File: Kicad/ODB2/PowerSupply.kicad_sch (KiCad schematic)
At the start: 54 parts, among them J2 Batt4v2, J3 Batt7V4, Q3 PJA3411_R1_00001, U2 TPS61201DRCR, U3 LM1085-5.0, U8 MCP1727-1802xMF

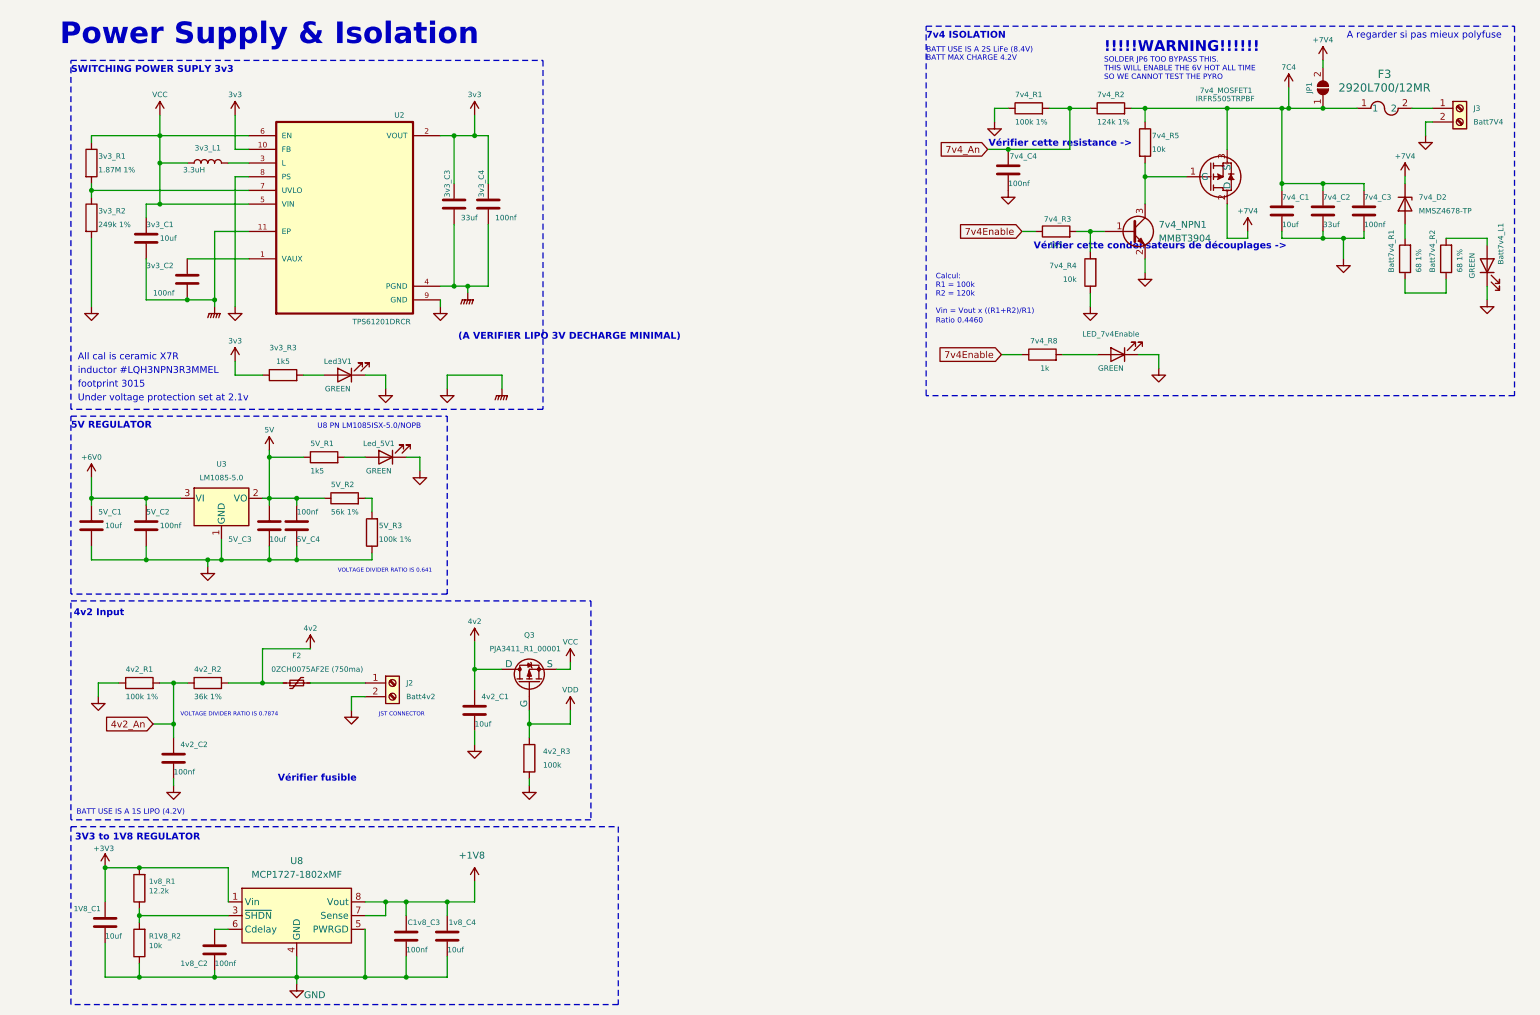
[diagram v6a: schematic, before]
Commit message: fixed r value
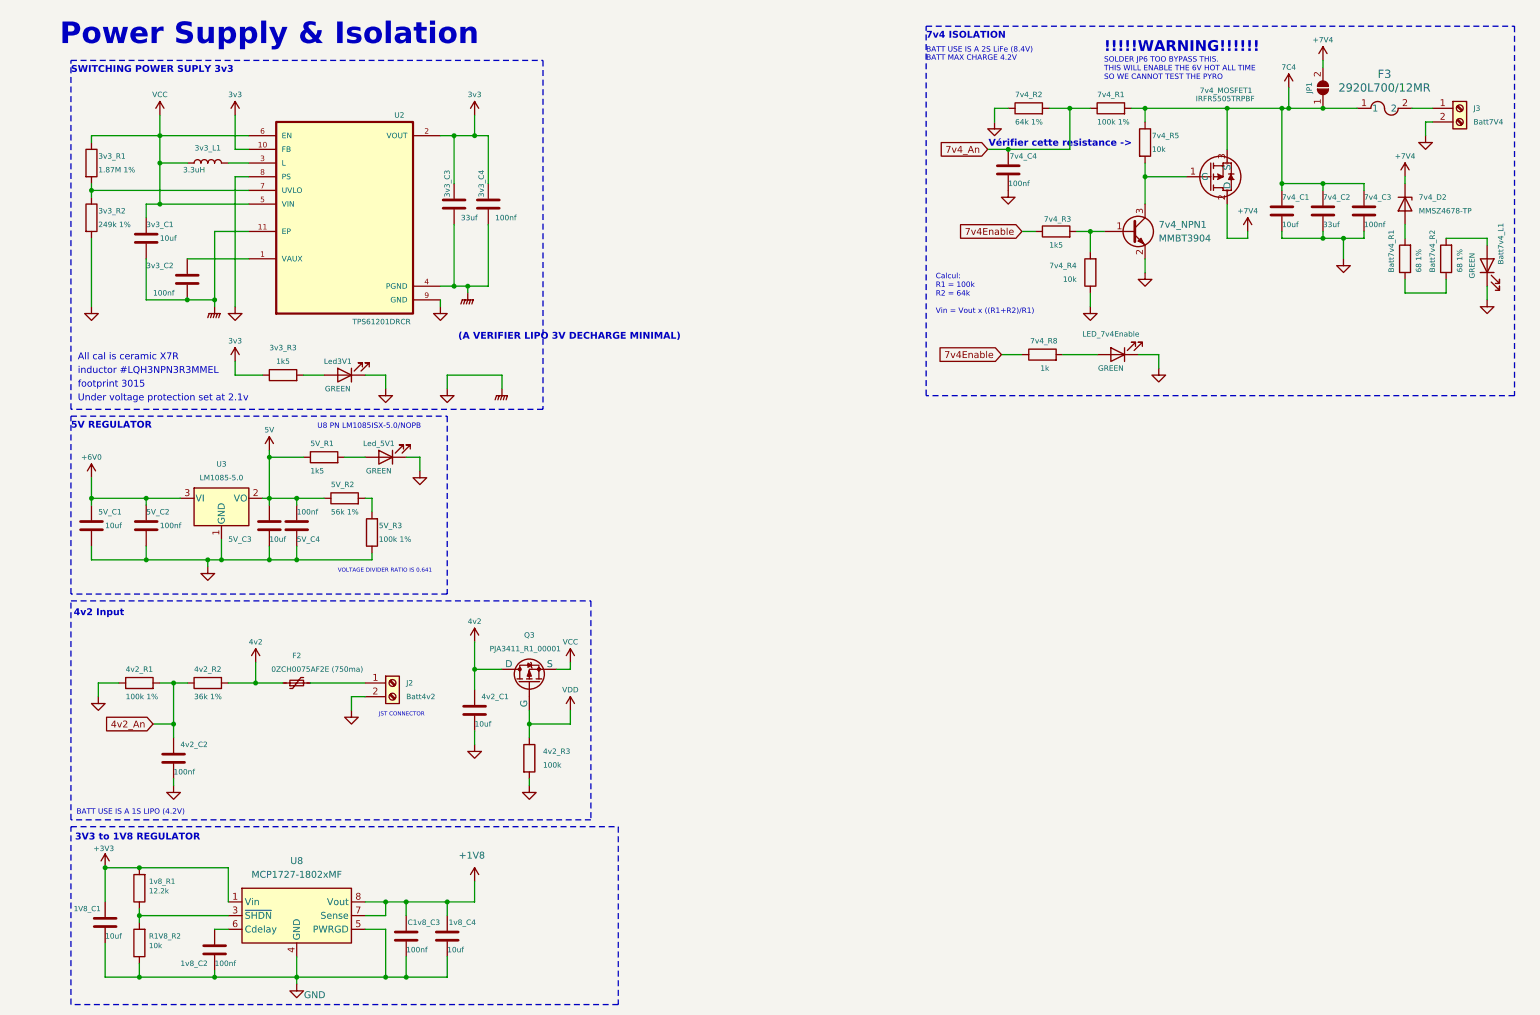
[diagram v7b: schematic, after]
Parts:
- 7v4_R1: renamed from 7v4_R2; value 124k 1% -> 100k 1%
- 7v4_R2: renamed from 7v4_R1; value 100k 1% -> 64k 1%
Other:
- note added: "Calcul: R1 = 100k R2 = 64k Vin = Vout x ((R1+R2)/R1)"
- note removed: "A regarder si pas mieux polyfuse"
- note removed: "Calcul: R1 = 100k R2 = 120k Vin = Vout x ((R1+R2)/R1)"
- note removed: "Ratio 0.4460"
- note removed: "VOLTAGE DIVIDER RATIO IS 0.7874"
- note removed: "Vérifier cette condensateurs de découplages ->"
- note removed: "Vérifier fusible"
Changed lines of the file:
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@@
 	)
 	(junction
+		(at 73.66 191.77)
+		(diameter 0)
+		(color 0 0 0 0)
+	)
+	(junction
 		(at 19.05 102.87)
 		(diameter 0)
@@
 	)
 	(junction
-		(at 69.85 191.77)
-		(diameter 0)
-		(color 0 0 0 0)
-	)
-	(junction
 		(at 200.66 30.48)
 		(diameter 0)
@@
 	)
 	(junction
-		(at 50.8 137.16)
+		(at 49.53 137.16)
 		(diameter 0)
 		(color 0 0 0 0)
@@
 	(wire
 		(pts
-			(xy 69.85 191.77) (xy 57.15 191.77)
+			(xy 57.15 191.77) (xy 73.66 191.77)
 		)
 		(stroke
@@
 	(wire
 		(pts
-			(xy 50.8 130.81) (xy 50.8 137.16)
+			(xy 49.53 133.35) (xy 49.53 137.16)
 		)
 		(stroke
@@
 	(wire
 		(pts
-			(xy 50.8 130.81) (xy 59.69 130.81)
-		)
-		(stroke
-			(width 0)
-			(type default)
-		)
-	)
-	(wire
-		(pts
 			(xy 262.89 64.77) (xy 262.89 62.23)
 		)
@@
 	(wire
 		(pts
-			(xy 77.47 191.77) (xy 69.85 191.77)
+			(xy 77.47 191.77) (xy 73.66 191.77)
 		)
 		(stroke
@@
 	(wire
 		(pts
-			(xy 44.45 137.16) (xy 50.8 137.16)
+			(xy 44.45 137.16) (xy 49.53 137.16)
+		)
+		(stroke
+			(width 0)
+			(type default)
+		)
+	)
+	(wire
+		(pts
+			(xy 73.66 182.88) (xy 69.85 182.88)
 		)
 		(stroke
@@
 	(wire
 		(pts
-			(xy 69.85 182.88) (xy 69.85 191.77)
+			(xy 73.66 182.88) (xy 73.66 191.77)
 		)
 		(stroke
@@
 	(wire
 		(pts
-			(xy 50.8 137.16) (xy 54.61 137.16)
+			(xy 49.53 137.16) (xy 54.61 137.16)
 		)
 		(stroke
@@
 		)
 	)
-	(text "Calcul: \nR1 = 100k\nR2 = 120k\n\nVin = Vout x ((R1+R2)/R1)"
+	(text "Calcul: \nR1 = 100k\nR2 = 64k\n\nVin = Vout x ((R1+R2)/R1)"
 		(exclude_from_sim no)
 		(at 175.768 68.834 0)
@@
 		)
 	)
-	(text "Vérifier fusible"
-		(exclude_from_sim no)
-		(at 60.96 154.94 0)
-		(effects
-			(font
-				(size 1.27 1.27)
-				(thickness 0.254)
-				(bold yes)
-			)
-		)
-	)
-	(text "Vérifier cette condensateurs de découplages ->"
-		(exclude_from_sim no)
-		(at 217.424 56.134 0)
-		(effects
-			(font
-				(size 1.27 1.27)
-				(thickness 0.254)
-				(bold yes)
-			)
-		)
-	)
 	(text "BATT USE IS A 1S LIPO (4.2V)"
 		(exclude_from_sim no)
@@
 		)
 	)
-	(text "VOLTAGE DIVIDER RATIO IS 0.7874"
-		(exclude_from_sim no)
-		(at 35.56 143.51 0)
-		(effects
-			(font
-				(size 0.75 0.75)
-			)
-			(justify left bottom)
-		)
-	)
 	(text "!!!!!WARNING!!!!!!"
 		(exclude_from_sim no)
@@
 		)
 	)
-	(text "Ratio 0.4460"
-		(exclude_from_sim no)
-		(at 175.768 70.612 0)
-		(effects
-			(font
-				(size 1 1)
-			)
-			(justify left bottom)
-		)
-	)
-	(text "A regarder si pas mieux polyfuse\n"
-		(exclude_from_sim no)
-		(at 266.446 17.018 0)
-		(effects
-			(font
-				(size 1.27 1.27)
-			)
-		)
-	)
 	(text "Vérifier cette resistance ->"
 		(exclude_from_sim no)
@@
 	(symbol
 		(lib_id "power:+BATT")
-		(at 59.69 130.81 0)
+		(at 49.53 133.35 0)
 		(unit 1)
 		(exclude_from_sim no)
@@
 		(dnp no)
 		(property "Reference" "#PWR021"
-			(at 59.69 134.62 0)
+			(at 49.53 137.16 0)
 			(effects
 				(font
@@
 		)
 		(property "Value" "4v2"
-			(at 59.69 127 0)
+			(at 49.53 129.54 0)
 			(effects
 				(font
@@
 		)
 		(property "Footprint" ""
-			(at 59.69 130.81 0)
+			(at 49.53 133.35 0)
 			(effects
 				(font
@@
 		)
 		(property "Datasheet" ""
-			(at 59.69 130.81 0)
+			(at 49.53 133.35 0)
 			(effects
 				(font
@@
 		)
 		(property "Description" ""
-			(at 59.69 130.81 0)
+			(at 49.53 133.35 0)
 			(effects
 				(font
@@
 		(on_board yes)
 		(dnp no)
-		(property "Reference" "7v4_R1"
+		(property "Reference" "7v4_R2"
 			(at 190.5 27.94 90)
 			(effects
@@
 			)
 		)
-		(property "Value" "100k 1%"
+		(property "Value" "64k 1%"
 			(at 190.5 33.02 90)
 			(effects
@@
 			(project "ODB2"
 				(path "/4b06c5d1-aa8b-48ed-8972-b43a60cfab78/a0dfa29e-ccca-4096-8481-c7e33c67aac5"
-					(reference "7v4_R1")
+					(reference "7v4_R2")
 					(unit 1)
 				)
@@
 		(on_board yes)
 		(dnp no)
-		(property "Reference" "7v4_R2"
+		(property "Reference" "7v4_R1"
 			(at 205.74 27.94 90)
 			(effects
@@
 			)
 		)
-		(property "Value" "124k 1%"
+		(property "Value" "100k 1%"
 			(at 205.74 33.02 90)
 			(effects
@@
 			(project "ODB2"
 				(path "/4b06c5d1-aa8b-48ed-8972-b43a60cfab78/a0dfa29e-ccca-4096-8481-c7e33c67aac5"
-					(reference "7v4_R2")
+					(reference "7v4_R1")
 					(unit 1)
 				)

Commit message: fix resistance 4v2 input + labels
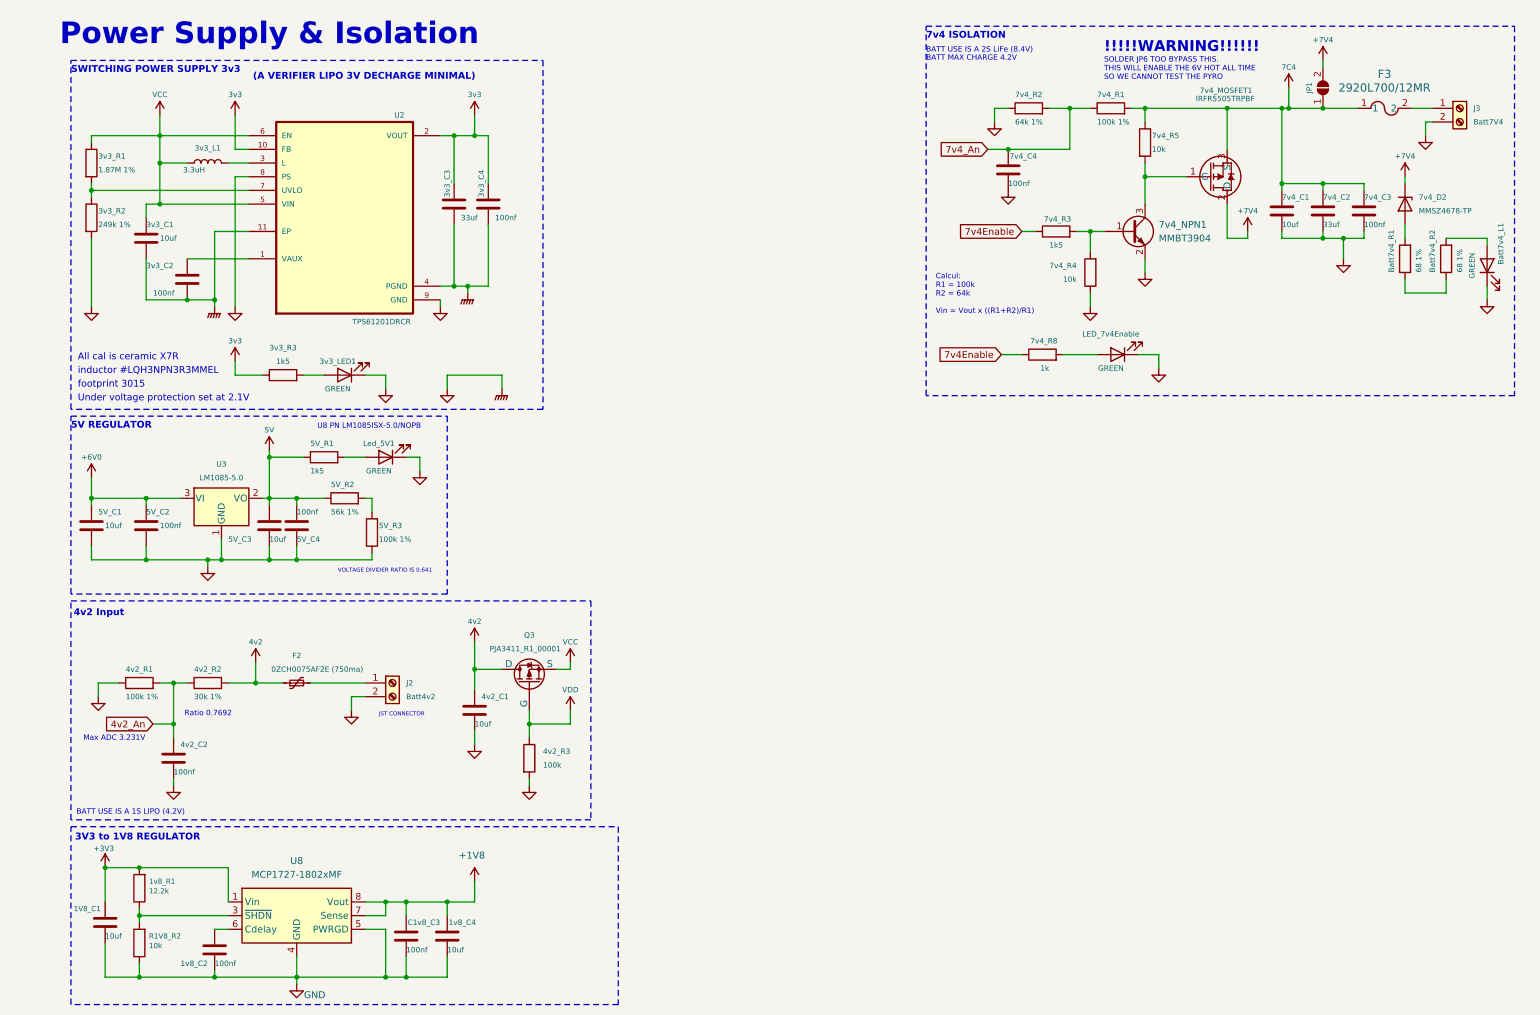
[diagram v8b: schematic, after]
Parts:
- 4v2_R2: value 36k 1% -> 30k 1%
- renumbered Led3V1 to 3v3_LED1
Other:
- note added: "Max ADC 3.231V"
- note added: "Ratio 0.7692"
- note added: "SWITCHING POWER SUPPLY 3v3"
- note added: "Under voltage protection set at 2.1V"
- note removed: "SWITCHING POWER SUPLY 3v3"
- note removed: "Under voltage protection set at 2.1v"
- note removed: "Vérifier cette resistance ->"
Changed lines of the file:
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@@
 		)
 	)
-	(text "Under voltage protection set at 2.1v"
+	(text "Under voltage protection set at 2.1V"
 		(exclude_from_sim no)
 		(at 16.51 85.09 0)
@@
 	(text "(A VERIFIER LIPO 3V DECHARGE MINIMAL)"
 		(exclude_from_sim no)
-		(at 87.122 73.66 0)
+		(at 49.022 25.4 0)
 		(effects
 			(font
@@
 		)
 	)
+	(text "Max ADC 3.231V"
+		(exclude_from_sim no)
+		(at 17.526 148.082 0)
+		(effects
+			(font
+				(size 1 1)
+				(thickness 0.125)
+			)
+			(justify left bottom)
+		)
+	)
 	(text "!!!!!WARNING!!!!!!"
 		(exclude_from_sim no)
@@
 		)
 	)
-	(text "SWITCHING POWER SUPLY 3v3"
+	(text "SWITCHING POWER SUPPLY 3v3"
 		(exclude_from_sim no)
 		(at 15.24 24.13 0)
@@
 		)
 	)
-	(text "Vérifier cette resistance ->"
-		(exclude_from_sim no)
-		(at 198.882 37.084 0)
-		(effects
-			(font
-				(size 1.27 1.27)
-				(thickness 0.254)
-				(bold yes)
-			)
-		)
-	)
 	(text "BATT USE IS A 2S LiFe (8.4V)"
 		(exclude_from_sim no)
@@
 		)
 	)
+	(text "Ratio 0.7692"
+		(exclude_from_sim no)
+		(at 36.322 143.51 0)
+		(effects
+			(font
+				(size 1 1)
+				(thickness 0.125)
+			)
+			(justify left bottom)
+		)
+	)
 	(text "VOLTAGE DIVIDER RATIO IS 0.641"
 		(exclude_from_sim no)
@@
 			)
 		)
-		(property "Value" "36k 1%"
+		(property "Value" "30k 1%"
 			(at 38.1 139.7 90)
 			(effects
@@
 		(on_board yes)
 		(dnp no)
-		(property "Reference" "Led3V1"
+		(property "Reference" "3v3_LED1"
 			(at 64.77 77.47 0)
 			(effects
@@
 			(project "ODB2"
 				(path "/4b06c5d1-aa8b-48ed-8972-b43a60cfab78/a0dfa29e-ccca-4096-8481-c7e33c67aac5"
-					(reference "Led3V1")
+					(reference "3v3_LED1")
 					(unit 1)
 				)
